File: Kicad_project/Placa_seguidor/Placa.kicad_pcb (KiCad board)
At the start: 2 copper layers, 30 parts, among them J1 Conn_01x02_Female, J2 Conn_01x08_Female, U1 barra2pins, U10 PW_Slinha, U13 Desenho_placa_seguidor, U2 barra3pins, U3 Borne, U4 Borne, U5 Borne, U6 Borne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

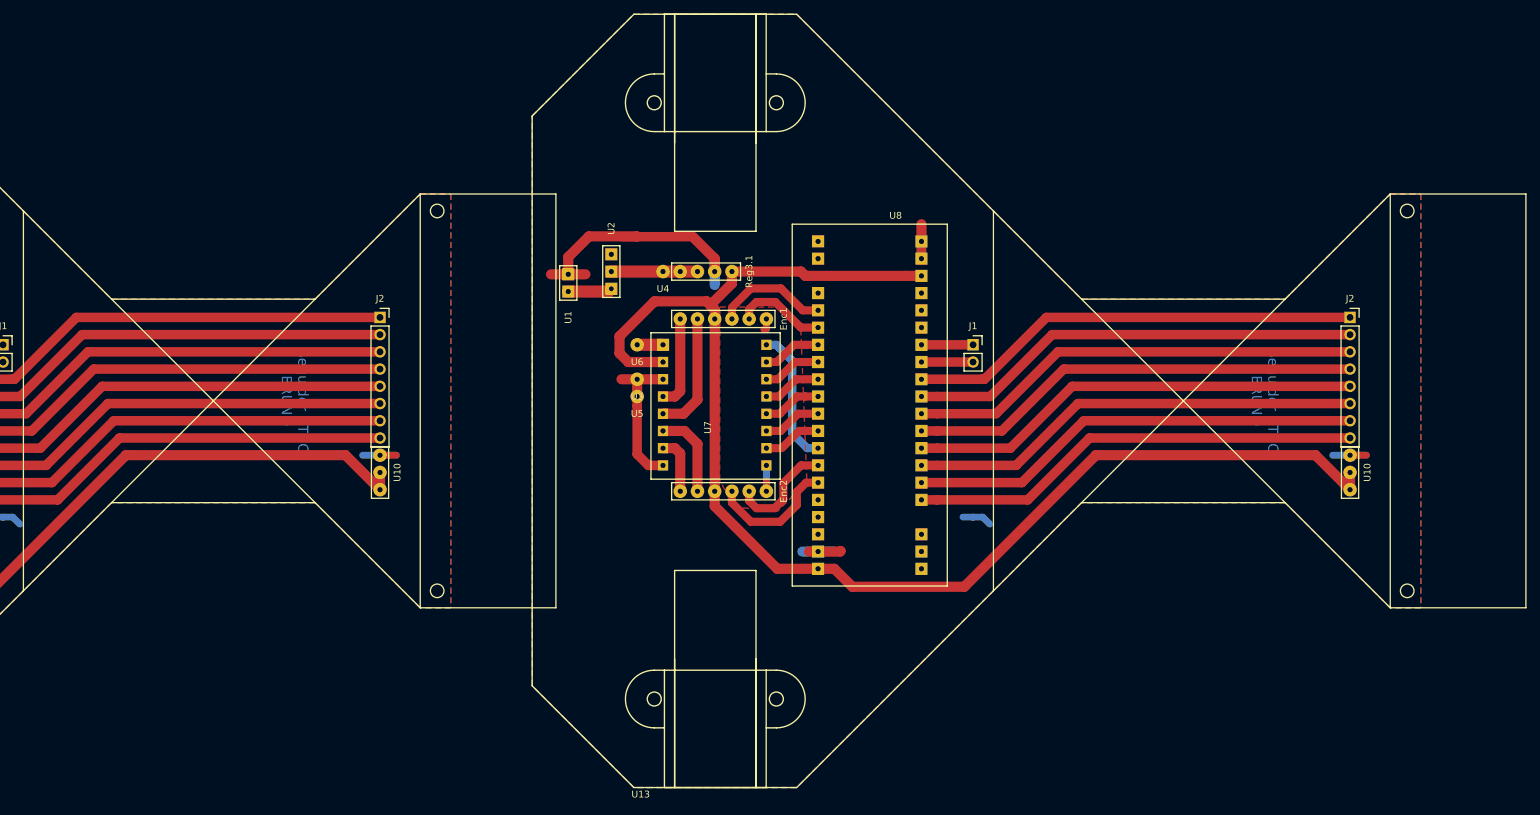
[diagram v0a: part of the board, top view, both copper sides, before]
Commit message: Testing reflectance sensor
Worked fine
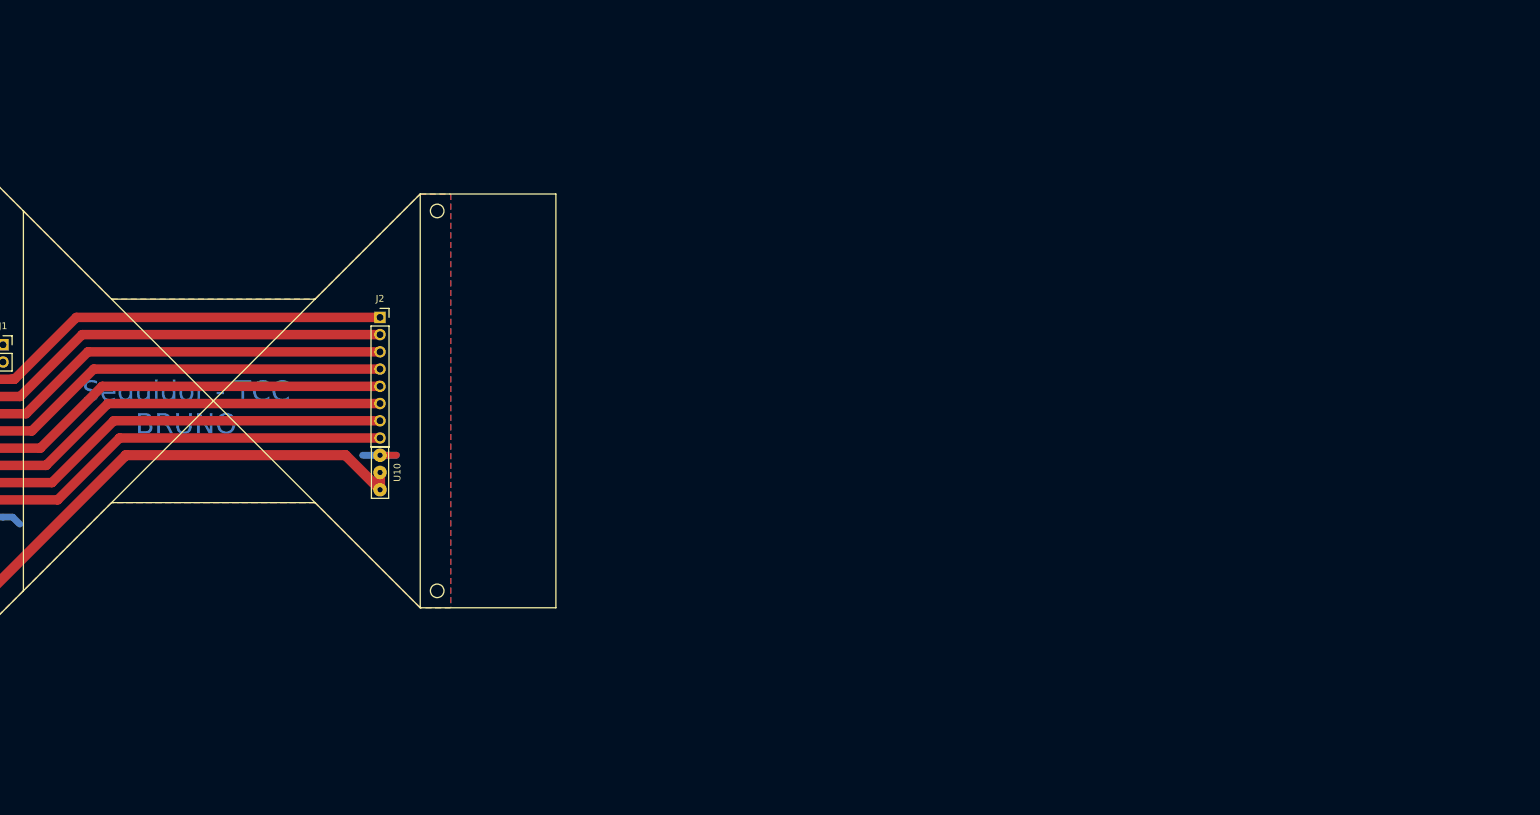
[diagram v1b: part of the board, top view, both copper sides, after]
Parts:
- removed the Enc1 at (182.4, 59.9)
- removed the Enc2 at (182.4, 85.3)
- removed the J1 at (223.0, 63.7)
- removed the J2 at (278.6, 59.7)
- removed the Reg3.1 at (182.4, 52.9)
- removed the U1 at (163.3, 55.9)
- removed the U10 at (278.6, 82.5)
- removed the U13 at (173.0, 129.0)
- removed the U2 at (169.7, 52.9)
- removed the U3 at (173.5, 68.8)
- removed the U4 at (177.3, 52.9)
- removed the U5 at (173.5, 71.3)
- removed the U6 at (173.5, 63.7)
- removed the U7 at (177.3, 61.2)
- removed the U8 at (205.2, 73.9)
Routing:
- net /V3.3: track 401.3 -> 200.6 mm
- net /GND: track 202.1 -> 101.1 mm
- net Net-(J2-Pad5): track 134.3 -> 67.2 mm
- net Net-(J2-Pad8): track 133.9 -> 67.0 mm
- net Net-(J2-Pad6): track 133.9 -> 67.0 mm
- net Net-(J2-Pad3): track 133.9 -> 67.0 mm
- net Net-(J2-Pad7): track 133.9 -> 67.0 mm
- net Net-(J2-Pad4): track 133.9 -> 67.0 mm
- net Net-(J2-Pad2): track 133.9 -> 67.0 mm
- net Net-(J2-Pad1): track 133.9 -> 67.0 mm
- net /PWM_E: track 40.4 -> 20.2 mm
- net /ENC_D_A: track 38.2 -> 19.1 mm
- net /A2: track 35.7 -> 17.8 mm
- net /ENC_E_A: track 33.8 -> 16.9 mm
- net /ENC_D_B: track 32.1 -> 16.0 mm
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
